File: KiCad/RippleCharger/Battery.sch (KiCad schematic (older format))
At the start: 45 parts, among them J5 bat+, J6 bat-, J7 Load, Q2 2N3904, Q3 TIP41C, Q4 2N3904, Q5 2N3904, Q6 2N3904, SW1 SW_SPDT, U8 INA282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

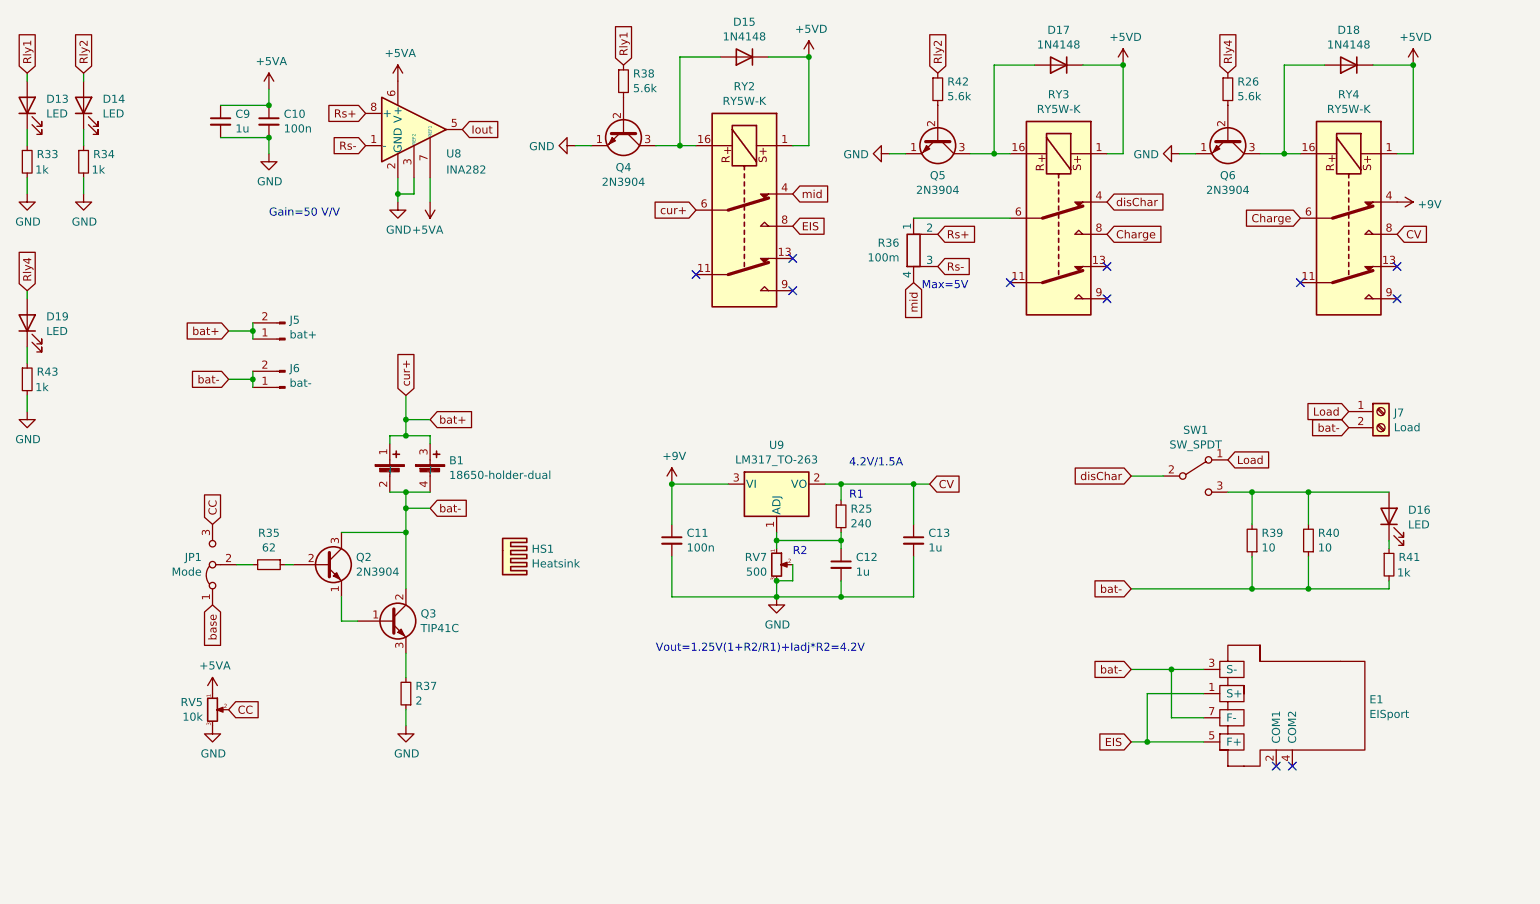
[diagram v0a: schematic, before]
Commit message: Update PCB layout m include relay footprint, board outlook.Modify Main 0049 code and add CV function
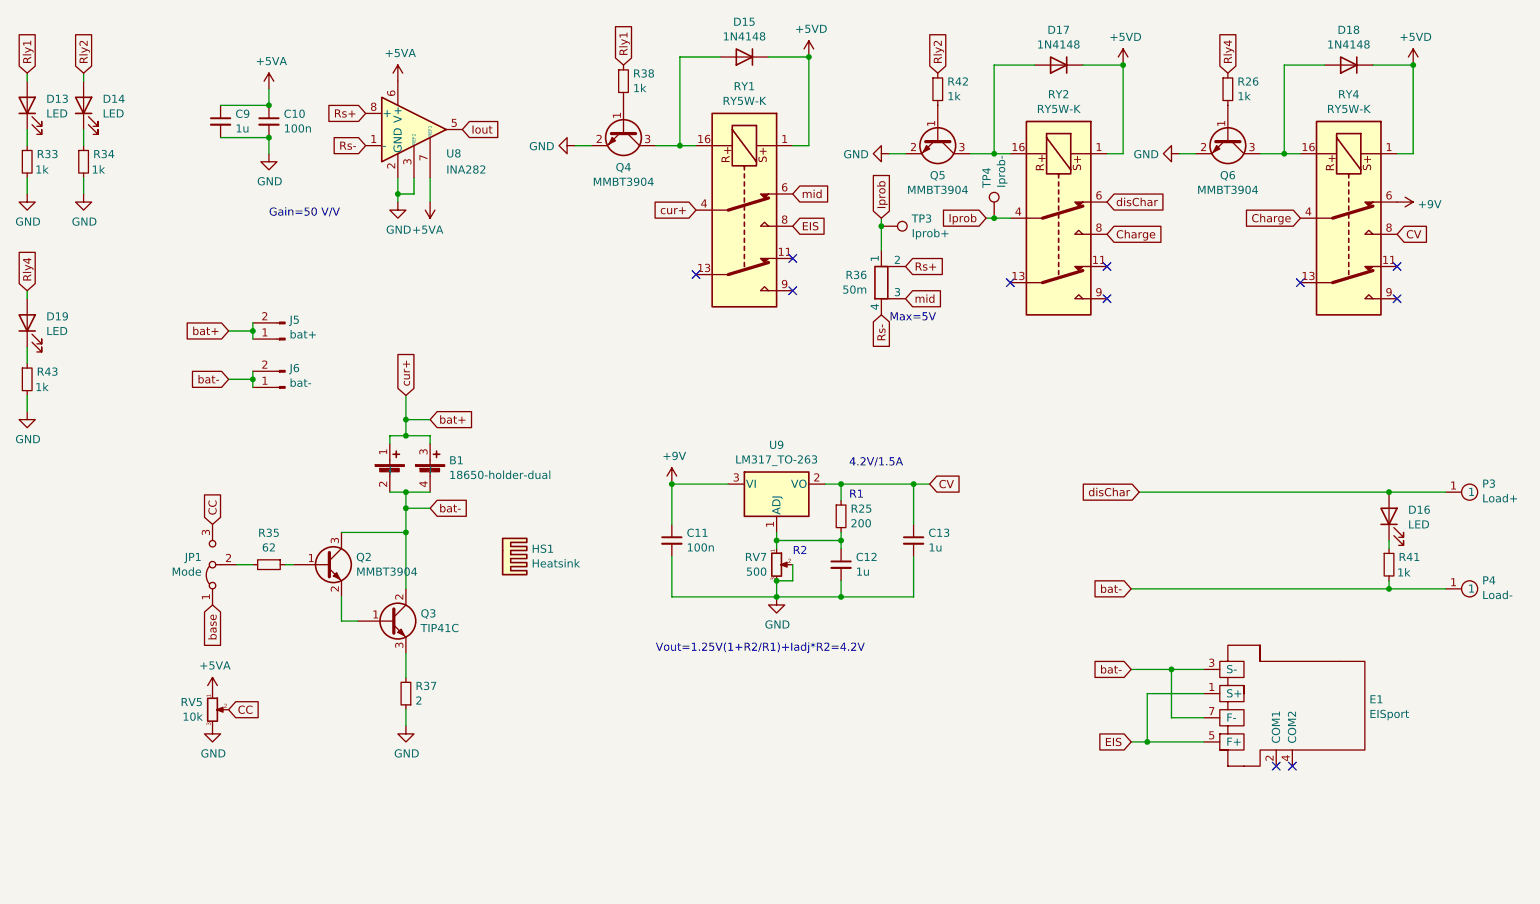
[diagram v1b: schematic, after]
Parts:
- removed J7: Load, TerminalBlock:TerminalBlock_Altech_AK300-2_P5.00mm, symbol Connector:Screw_Terminal_01x02
- removed Q2, Q4, Q5, Q6: 2N3904, Package_TO_SOT_SMD:SOT-23, symbol Transistor_BJT:2N3904
- removed R39, R40: 10, Resistor_THT:R_Axial_Power_L20.0mm_W6.4mm_P25.40mm, symbol Device:R_Small
- removed RY2, RY3, RY4: RY5W-K, basic:RY5W-K, symbol RippleCharger-rescue:RY5W-K-basic
- removed SW1: SW_SPDT, basic:MTS-102, symbol Switch:SW_SPDT
- added P3: Load+, basic:IOPad, symbol basic:IOPad
- added P4: Load-, basic:IOPad, symbol basic:IOPad
- added Q2, Q4, Q5, Q6: MMBT3904, Package_TO_SOT_SMD:SOT-23, symbol Transistor_BJT:MMBT3904
- added RY1, RY2, RY4: RY5W-K, basic:RY5W-K, symbol basic:RY5W-K
- added TP3: Iprob+, Connector_PinHeader_2.54mm:PinHeader_1x01_P2.54mm_Vertical, symbol Connector:TestPoint
- added TP4: Iprob-, Connector_PinHeader_2.54mm:PinHeader_1x01_P2.54mm_Vertical, symbol Connector:TestPoint
- D15, D17, D18: footprint Diode_SMD:D_0805_2012Metric_Pad1.15x1.40mm_HandSolder -> Diode_SMD:D_SOD-123
- R25: value 240 -> 200
- R26, R38, R42: value 5.6k -> 1k
- R36: value 100m -> 50m
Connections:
- net +5VD: now also RY1.1, RY2.1, RY4.1
- net +9V: now also RY4.6
- net CV: now also RY4.8
- net Charge: now also RY2.8, RY4.4
- net EIS: now also RY1.8
- net GND: now also Q4.2 (E), Q5.2 (E), Q6.2 (E)
- net Rs-: now also R36.4; no longer R36.3
- net bat+: now also RY1.4
- net bat-: now also P4.1, Q2.3 (C)
- net disChar: now also D16.2 (A), P3.1, RY2.6
- net mid: now also R36.3, RY1.6; no longer R36.4
- net at Q3.1 (B): now also Q2.2 (E)
- net at R35.1: now also Q2.1 (B)
- net at D17.2 (A): now also Q5.3 (C), RY2.16
- net Iprob: now reaches R36.1
- net Iprob: now also RY2.4, TP3.1, TP4.1
- net at R42.2: now also Q5.1 (B)
- net at D15.2 (A): now also Q4.3 (C), RY1.16
- net at R38.2: now also Q4.1 (B)
- net at R26.2: now also Q6.1 (B)
- net at D18.2 (A): now also Q6.3 (C), RY4.16
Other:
- moved on the sheet: R36

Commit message: Fix CV charging route
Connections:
- net GND: now also RY4.9
- net bat-: now also RY4.13; no longer Q2.3 (C), Q3.2 (C)
- net bat-2: now reaches RY4.11
- net bat-2: now also Q2.3 (C), Q3.2 (C)
- no-connect marks 11 -> 8
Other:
- moved on the sheet: JP1, Q2, Q3, R35, R37, RV5
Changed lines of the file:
@@
 Text GLabel 6600 2100 2    50   Input ~ 0
 mid
-Text GLabel 6000 2200 0    50   Input ~ 0
-cur+
 Connection ~ 6700 1250
 $Comp
@@
 Wire Wire Line
 	4200 3500 4200 3600
-Connection ~ 4200 3500
 Wire Wire Line
 	4350 3500 4200 3500
-Wire Wire Line
-	4200 4050 4200 4200
-Connection ~ 4200 4050
-Wire Wire Line
-	4350 4050 4200 4050
-Text GLabel 4350 4050 2    50   Input ~ 0
-bat-
 Text GLabel 4350 3500 2    50   Input ~ 0
 bat+
@@
 Connection ~ 4200 3600
 Wire Wire Line
-	4200 3950 4200 4050
-$Comp
-L RippleCharger-rescue:18650-holder-dual-basic B1
-U 1 1 6136FA5A
-P 4200 4250
-AR Path="/6136FA5A" Ref="B1"  Part="1"
-AR Path="/613448A2/6136FA5A" Ref="B1"  Part="1"
-F 0 "B1" H 4468 4746 50  0000 L CNN
-F 1 "18650-holder-dual" H 4468 4655 50  0000 L CNN
-F 2 "basic:18650-holder-dual" H 4200 4250 50  0001 C CNN
-F 3 "" H 4200 4250 50  0001 C CNN
-	1    4200 4250
-	1    0    0    -1
-$EndComp
-Wire Wire Line
-	4200 3950 4350 3950
-Text GLabel 3000 4150 1    50   Input ~ 0
-CC
-$Comp
-L Jumper:Jumper_3_Bridged12 JP1
-U 1 1 613B215C
-P 3000 4400
-F 0 "JP1" V 3046 4467 50  0000 L CNN
-F 1 "Mode" V 2955 4467 50  0000 L CNN
-F 2 "Connector_PinHeader_2.54mm:PinHeader_1x03_P2.54mm_Vertical" H 3000 4400 50  0001 C CNN
-F 3 "~" H 3000 4400 50  0001 C CNN
-	1    3000 4400
-	0    -1   -1   0
-$EndComp
-Wire Wire Line
-	3250 4400 3150 4400
-Wire Wire Line
-	3450 4400 3500 4400
-Text GLabel 3000 4650 3    50   Input ~ 0
-base
-Wire Wire Line
 	4350 3600 4350 3650
 Wire Wire Line
 	4100 3600 4100 3650
-Connection ~ 4200 4200
-Wire Wire Line
-	4200 4550 4200 4200
-Connection ~ 4200 3950
-Wire Wire Line
-	4100 3950 4200 3950
-Wire Wire Line
-	4200 5400 4200 5300
-$Comp
-L power:GND #PWR053
-U 1 1 6138F10D
-P 4200 5400
-F 0 "#PWR053" H 4200 5150 50  0001 C CNN
-F 1 "GND" H 4205 5227 50  0000 C CNN
-F 2 "" H 4200 5400 50  0001 C CNN
-F 3 "" H 4200 5400 50  0001 C CNN
-	1    4200 5400
-	1    0    0    -1
-$EndComp
-Wire Wire Line
-	3800 4200 4200 4200
-Wire Wire Line
-	4200 4950 4200 5100
-Wire Wire Line
-	3800 4750 3900 4750
-Wire Wire Line
-	3800 4600 3800 4750
-$Comp
-L Device:R_Small R37
-U 1 1 61378561
-P 4200 5200
-F 0 "R37" H 4141 5154 50  0000 R CNN
-F 1 "2" H 4141 5245 50  0000 R CNN
-F 2 "Resistor_THT:R_Axial_Power_L20.0mm_W6.4mm_P25.40mm" H 4200 5200 50  0001 C CNN
-F 3 "~" H 4200 5200 50  0001 C CNN
-	1    4200 5200
-	-1   0    0    1
-$EndComp
-$Comp
-L Device:R_Small R35
-U 1 1 61377410
-P 3350 4400
-F 0 "R35" V 3154 4400 50  0000 C CNN
-F 1 "62" V 3245 4400 50  0000 C CNN
-F 2 "Resistor_SMD:R_0805_2012Metric_Pad1.20x1.40mm_HandSolder" H 3350 4400 50  0001 C CNN
-F 3 "~" H 3350 4400 50  0001 C CNN
-	1    3350 4400
-	0    1    1    0
-$EndComp
 $Comp
 L Mechanical:Heatsink HS1
@@
 	1    4800 4350
 	0    1    1    0
-$EndComp
-$Comp
-L Transistor_BJT:TIP41C Q3
-U 1 1 61373007
-P 4100 4750
-F 0 "Q3" H 4291 4796 50  0000 L CNN
-F 1 "TIP41C" H 4291 4705 50  0000 L CNN
-F 2 "Package_TO_SOT_THT:TO-220-3_Vertical" H 4350 4675 50  0001 L CIN
-F 3 "https://www.centralsemi.com/get_document.php?cmp=1&mergetype=pd&mergepath=pd&pdf_id=tip41.PDF" H 4100 4750 50  0001 L CNN
-	1    4100 4750
-	1    0    0    -1
-$EndComp
-$Comp
-L Device:R_POT_Small RV5
-U 1 1 61438FD4
-P 3000 5300
-F 0 "RV5" H 2940 5346 50  0000 R CNN
-F 1 "10k" H 2940 5255 50  0000 R CNN
-F 2 "Potentiometer_THT:Potentiometer_Bourns_3296W_Vertical" H 3000 5300 50  0001 C CNN
-F 3 "~" H 3000 5300 50  0001 C CNN
-	1    3000 5300
-	1    0    0    -1
-$EndComp
-$Comp
-L power:+5VA #PWR047
-U 1 1 6143AC0B
-P 3000 5200
-F 0 "#PWR047" H 3000 5050 50  0001 C CNN
-F 1 "+5VA" H 3015 5373 50  0000 C CNN
-F 2 "" H 3000 5200 50  0001 C CNN
-F 3 "" H 3000 5200 50  0001 C CNN
-	1    3000 5200
-	1    0    0    -1
-$EndComp
-Text GLabel 3100 5300 2    50   Input ~ 0
-CC
-$Comp
-L power:GND #PWR048
-U 1 1 6143A03A
-P 3000 5400
-F 0 "#PWR048" H 3000 5150 50  0001 C CNN
-F 1 "GND" H 3005 5227 50  0000 C CNN
-F 2 "" H 3000 5400 50  0001 C CNN
-F 3 "" H 3000 5400 50  0001 C CNN
-	1    3000 5400
-	1    0    0    -1
 $EndComp
 Text GLabel 8750 3950 0    50   Input ~ 0
@@
 Text Notes 7200 2900 0    50   ~ 0
 Max=5V
-Text GLabel 4200 3350 1    50   Input ~ 0
-cur+
 $Comp
 L Amplifier_Current:INA282 U8
@@
 	1    0    0    -1
 $EndComp
-Wire Wire Line
-	4200 3350 4200 3500
 Text GLabel 7300 2750 2    50   Input ~ 0
 mid
@@
 	-1   0    0    1
 $EndComp
-NoConn ~ 10350 2550
-NoConn ~ 10350 2750
-NoConn ~ 9750 2650
 Text GLabel 9750 2250 0    50   Input ~ 0
 Charge
@@
 $EndComp
 $Comp
-L Transistor_BJT:MMBT3904 Q2
-U 1 1 6168CA9B
-P 3700 4400
-F 0 "Q2" H 3891 4446 50  0000 L CNN
-F 1 "MMBT3904" H 3891 4355 50  0000 L CNN
-F 2 "Package_TO_SOT_SMD:SOT-23" H 3900 4325 50  0001 L CIN
-F 3 "https://www.onsemi.com/pub/Collateral/2N3903-D.PDF" H 3700 4400 50  0001 L CNN
-	1    3700 4400
-	1    0    0    -1
-$EndComp
-$Comp
 L basic:RY5W-K RY1
 U 1 1 616C8532
@@
 Wire Wire Line
 	10300 3950 10650 3950
+$Comp
+L Transistor_BJT:MMBT3904 Q2
+U 1 1 6168CA9B
+P 3700 5200
+F 0 "Q2" H 3891 5246 50  0000 L CNN
+F 1 "MMBT3904" H 3891 5155 50  0000 L CNN
+F 2 "Package_TO_SOT_SMD:SOT-23" H 3900 5125 50  0001 L CIN
+F 3 "https://www.onsemi.com/pub/Collateral/2N3903-D.PDF" H 3700 5200 50  0001 L CNN
+	1    3700 5200
+	1    0    0    -1
+$EndComp
+$Comp
+L power:GND #PWR048
+U 1 1 6143A03A
+P 3000 6200
+F 0 "#PWR048" H 3000 5950 50  0001 C CNN
+F 1 "GND" H 3005 6027 50  0000 C CNN
+F 2 "" H 3000 6200 50  0001 C CNN
+F 3 "" H 3000 6200 50  0001 C CNN
+	1    3000 6200
+	1    0    0    -1
+$EndComp
+Text GLabel 3100 6100 2    50   Input ~ 0
+CC
+$Comp
+L power:+5VA #PWR047
+U 1 1 6143AC0B
+P 3000 6000
+F 0 "#PWR047" H 3000 5850 50  0001 C CNN
+F 1 "+5VA" H 3015 6173 50  0000 C CNN
+F 2 "" H 3000 6000 50  0001 C CNN
+F 3 "" H 3000 6000 50  0001 C CNN
+	1    3000 6000
+	1    0    0    -1
+$EndComp
+$Comp
+L Device:R_POT_Small RV5
+U 1 1 61438FD4
+P 3000 6100
+F 0 "RV5" H 2940 6146 50  0000 R CNN
+F 1 "10k" H 2940 6055 50  0000 R CNN
+F 2 "Potentiometer_THT:Potentiometer_Bourns_3296W_Vertical" H 3000 6100 50  0001 C CNN
+F 3 "~" H 3000 6100 50  0001 C CNN
+	1    3000 6100
+	1    0    0    -1
+$EndComp
+$Comp
+L Transistor_BJT:TIP41C Q3
+U 1 1 61373007
+P 4100 5550
+F 0 "Q3" H 4291 5596 50  0000 L CNN
+F 1 "TIP41C" H 4291 5505 50  0000 L CNN
+F 2 "Package_TO_SOT_THT:TO-220-3_Vertical" H 4350 5475 50  0001 L CIN
+F 3 "https://www.centralsemi.com/get_document.php?cmp=1&mergetype=pd&mergepath=pd&pdf_id=tip41.PDF" H 4100 5550 50  0001 L CNN
+	1    4100 5550
+	1    0    0    -1
+$EndComp
+$Comp
+L Device:R_Small R35
+U 1 1 61377410
+P 3350 5200
+F 0 "R35" V 3154 5200 50  0000 C CNN
+F 1 "62" V 3245 5200 50  0000 C CNN
+F 2 "Resistor_SMD:R_0805_2012Metric_Pad1.20x1.40mm_HandSolder" H 3350 5200 50  0001 C CNN
+F 3 "~" H 3350 5200 50  0001 C CNN
+	1    3350 5200
+	0    1    1    0
+$EndComp
+$Comp
+L Device:R_Small R37
+U 1 1 61378561
+P 4200 6000
+F 0 "R37" H 4141 5954 50  0000 R CNN
+F 1 "2" H 4141 6045 50  0000 R CNN
+F 2 "Resistor_THT:R_Axial_Power_L20.0mm_W6.4mm_P25.40mm" H 4200 6000 50  0001 C CNN
+F 3 "~" H 4200 6000 50  0001 C CNN
+	1    4200 6000
+	-1   0    0    1
+$EndComp
+Wire Wire Line
+	3800 5400 3800 5550
+Wire Wire Line
+	3800 5550 3900 5550
+Wire Wire Line
+	4200 5750 4200 5900
+Wire Wire Line
+	3800 5000 4200 5000
+$Comp
+L power:GND #PWR053
+U 1 1 6138F10D
+P 4200 6200
+F 0 "#PWR053" H 4200 5950 50  0001 C CNN
+F 1 "GND" H 4205 6027 50  0000 C CNN
+F 2 "" H 4200 6200 50  0001 C CNN
+F 3 "" H 4200 6200 50  0001 C CNN
+	1    4200 6200
+	1    0    0    -1
+$EndComp
+Wire Wire Line
+	4200 6200 4200 6100
+Wire Wire Line
+	4100 3950 4200 3950
+Connection ~ 4200 3950
+Wire Wire Line
+	4200 5350 4200 5000
+Text GLabel 3000 5450 3    50   Input ~ 0
+base
+Wire Wire Line
+	3450 5200 3500 5200
+Wire Wire Line
+	3250 5200 3150 5200
+$Comp
+L Jumper:Jumper_3_Bridged12 JP1
+U 1 1 613B215C
+P 3000 5200
+F 0 "JP1" V 3046 5267 50  0000 L CNN
+F 1 "Mode" V 2955 5267 50  0000 L CNN
+F 2 "Connector_PinHeader_2.54mm:PinHeader_1x03_P2.54mm_Vertical" H 3000 5200 50  0001 C CNN
+F 3 "~" H 3000 5200 50  0001 C CNN
+	1    3000 5200
+	0    -1   -1   0
+$EndComp
+Text GLabel 3000 4950 1    50   Input ~ 0
+CC
+Wire Wire Line
+	4200 3950 4350 3950
+$Comp
+L RippleCharger-rescue:18650-holder-dual-basic B1
+U 1 1 6136FA5A
+P 4200 4250
+AR Path="/6136FA5A" Ref="B1"  Part="1"
+AR Path="/613448A2/6136FA5A" Ref="B1"  Part="1"
+F 0 "B1" H 4468 4746 50  0000 L CNN
+F 1 "18650-holder-dual" H 4468 4655 50  0000 L CNN
+F 2 "basic:18650-holder-dual" H 4200 4250 50  0001 C CNN
+F 3 "" H 4200 4250 50  0001 C CNN
+	1    4200 4250
+	1    0    0    -1
+$EndComp
+Wire Wire Line
+	4200 3950 4200 4050
+Text GLabel 4350 4050 2    50   Input ~ 0
+bat-
+Wire Wire Line
+	4350 4050 4200 4050
+Text GLabel 6000 2200 0    50   Input ~ 0
+bat+
+Text GLabel 9750 2650 0    50   Input ~ 0
+bat-
+Text GLabel 4200 5000 1    50   Input ~ 0
+bat-2
+Text GLabel 10350 2550 2    50   Input ~ 0
+bat-2
+$Comp
+L power:GND #PWR0102
+U 1 1 616A3F3D
+P 10350 2750
+F 0 "#PWR0102" H 10350 2500 50  0001 C CNN
+F 1 "GND" H 10355 2577 50  0000 C CNN
+F 2 "" H 10350 2750 50  0001 C CNN
+F 3 "" H 10350 2750 50  0001 C CNN
+	1    10350 2750
+	0    -1   -1   0
+$EndComp
 $EndSCHEMATC

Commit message: Fix Layout error and adjust firmware ADC tradshold
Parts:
- added R?: 13m, Resistor_SMD:R_Shunt_Ohmite_LVK24, symbol Device:R_Shunt
- Q3: value TIP41C -> TIP31C
- R25: value 200 -> 180
- R36: value 50m -> 13m
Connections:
- net CV: no longer R25.1
- net Iprob: now also R?.4
- net Rs-: now also R?.1
- net bat+: now also R25.1
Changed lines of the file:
@@
 P 7150 2650
 F 0 "R36" H 7062 2696 50  0000 R CNN
-F 1 "50m" H 7062 2605 50  0000 R CNN
+F 1 "13m" H 7062 2605 50  0000 R CNN
 F 2 "Resistor_SMD:R_Shunt_Ohmite_LVK24" V 7080 2650 50  0001 C CNN
 F 3 "~" H 7150 2650 50  0001 C CNN
@@
 P 6900 4100
 F 0 "R25" H 6959 4146 50  0000 L CNN
-F 1 "200" H 6959 4055 50  0000 L CNN
+F 1 "180" H 6959 4055 50  0000 L CNN
 F 2 "Resistor_SMD:R_0805_2012Metric_Pad1.20x1.40mm_HandSolder" H 6900 4100 50  0001 C CNN
 F 3 "~" H 6900 4100 50  0001 C CNN
@@
 $EndComp
 Wire Wire Line
-	6800 3900 6900 3900
-Wire Wire Line
-	6900 4000 6900 3900
-Connection ~ 6900 3900
-Wire Wire Line
 	6500 4200 6500 4250
 Wire Wire Line
@@
 Wire Wire Line
 	7350 3900 7350 4150
-Wire Wire Line
-	6900 3900 7350 3900
 Wire Wire Line
 	7350 4350 7350 4600
@@
 Iprob
 Wire Wire Line
-	7150 2450 7150 2300
-Wire Wire Line
 	7800 2250 7850 2250
 $Comp
@@
 P 4100 5550
 F 0 "Q3" H 4291 5596 50  0000 L CNN
-F 1 "TIP41C" H 4291 5505 50  0000 L CNN
+F 1 "TIP31C" H 4291 5505 50  0000 L CNN
 F 2 "Package_TO_SOT_THT:TO-220-3_Vertical" H 4350 5475 50  0001 L CIN
 F 3 "https://www.centralsemi.com/get_document.php?cmp=1&mergetype=pd&mergepath=pd&pdf_id=tip41.PDF" H 4100 5550 50  0001 L CNN
@@
 	0    -1   -1   0
 $EndComp
+Wire Wire Line
+	6800 3900 7350 3900
+Text GLabel 6900 3850 1    50   Input ~ 0
+bat+
+Wire Wire Line
+	6900 3850 6900 4000
+$Comp
+L Device:R_Shunt R?
+U 1 1 61744249
+P 6850 2650
+F 0 "R?" H 6762 2696 50  0000 R CNN
+F 1 "13m" H 6762 2605 50  0000 R CNN
+F 2 "Resistor_SMD:R_Shunt_Ohmite_LVK24" V 6780 2650 50  0001 C CNN
+F 3 "~" H 6850 2650 50  0001 C CNN
+	1    6850 2650
+	1    0    0    1
+$EndComp
+Wire Wire Line
+	6850 2450 6850 2300
+Wire Wire Line
+	6850 2300 7150 2300
+Connection ~ 7150 2350
+Wire Wire Line
+	7150 2350 7150 2300
+Wire Wire Line
+	6850 2850 7150 2850
+Wire Wire Line
+	7150 2300 7150 2450
 $EndSCHEMATC
